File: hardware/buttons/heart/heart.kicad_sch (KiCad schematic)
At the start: 10 parts

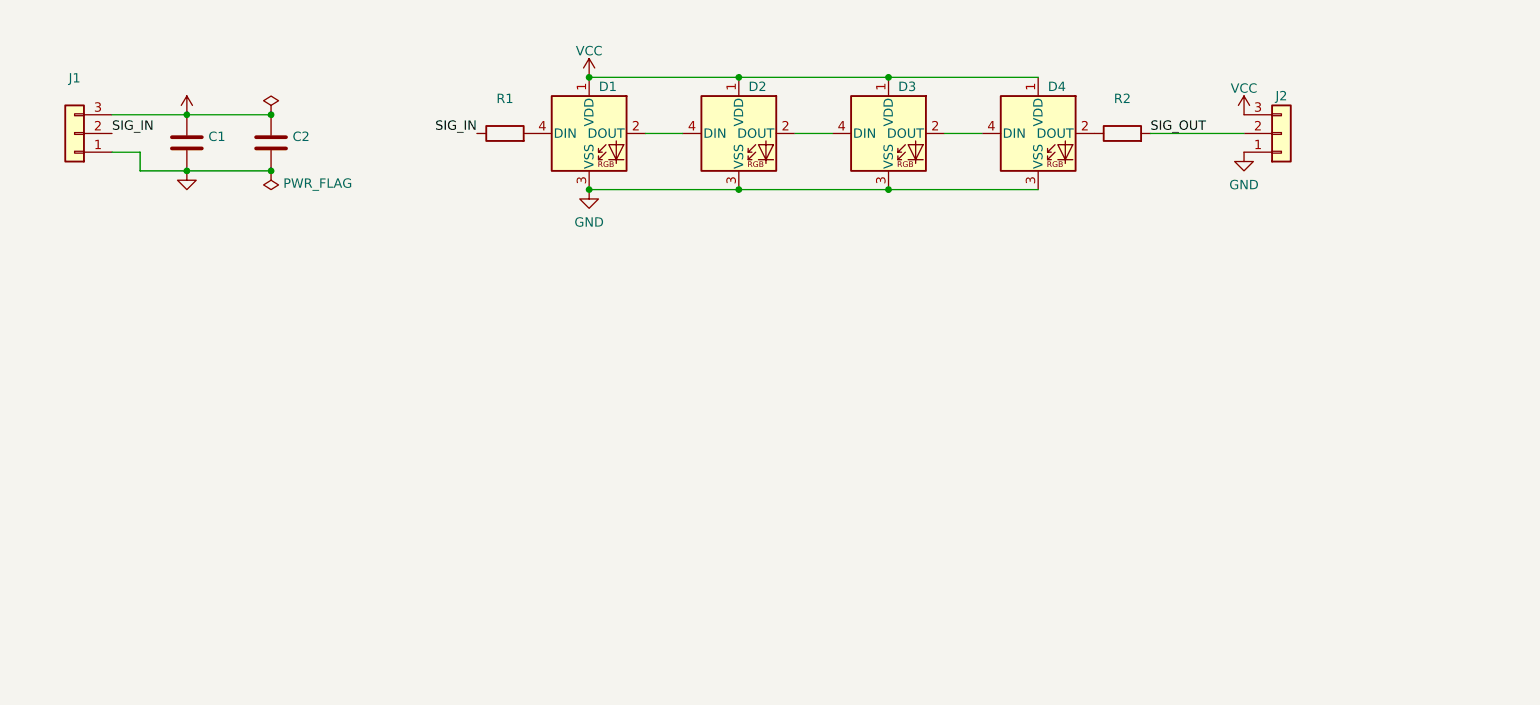
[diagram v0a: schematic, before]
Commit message: Add heart button
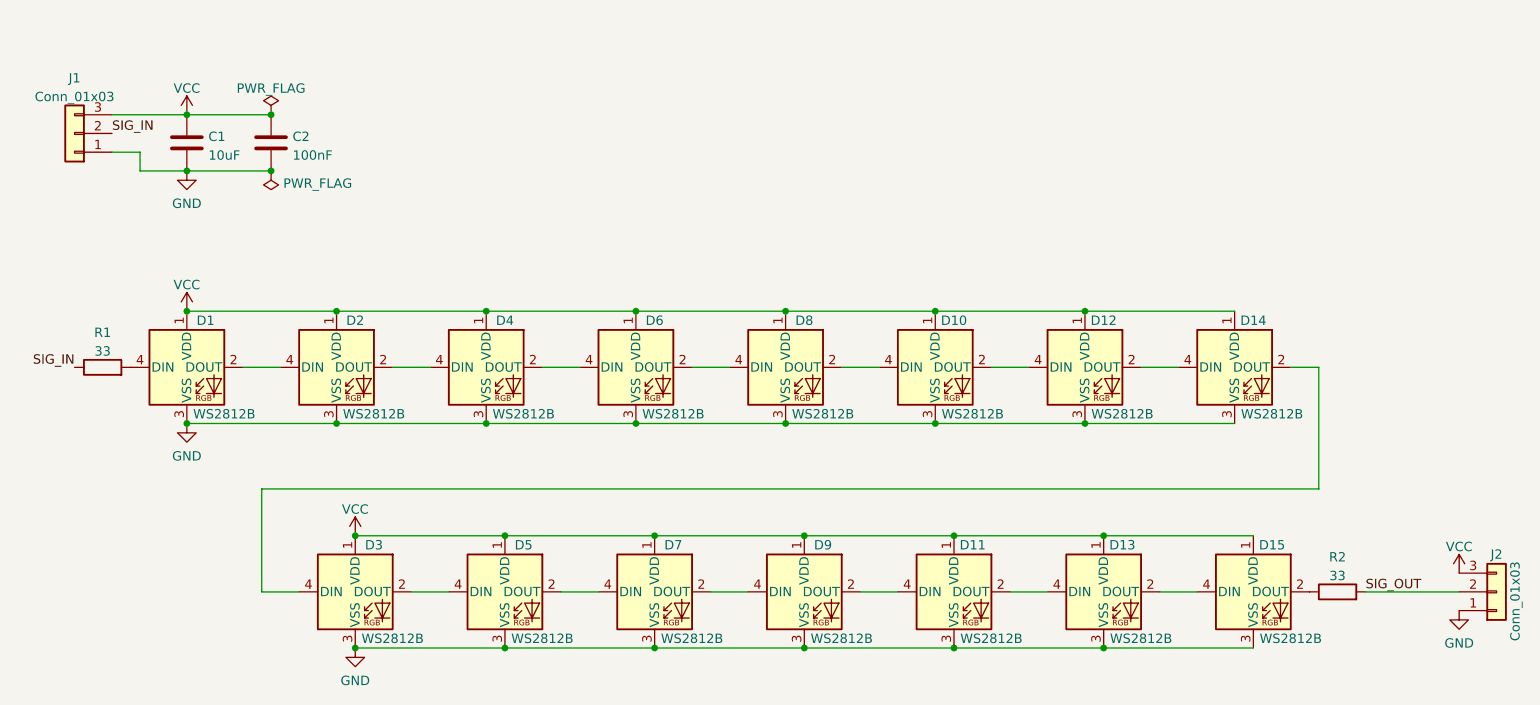
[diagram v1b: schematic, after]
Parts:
- added D10, D11, D12, D13, D14, D15, D3, D5, D7, D8, D9: WS2812B, LED_SMD:LED_WS2812B_PLCC4_5.0x5.0mm_P3.2mm, symbol LED:WS2812B
- C1: value (none) -> 10uF; footprint (none) -> Capacitor_SMD:C_0603_1608Metric
- C2: value (none) -> 100nF; footprint (none) -> Capacitor_SMD:C_0402_1005Metric
- D1, D2: value (none) -> WS2812B; footprint (none) -> LED_SMD:LED_WS2812B_PLCC4_5.0x5.0mm_P3.2mm
- D4: renamed from D3; value (none) -> WS2812B; footprint (none) -> LED_SMD:LED_WS2812B_PLCC4_5.0x5.0mm_P3.2mm
- D6: renamed from D4; value (none) -> WS2812B; footprint (none) -> LED_SMD:LED_WS2812B_PLCC4_5.0x5.0mm_P3.2mm
- J1, J2: value (none) -> Conn_01x03; footprint (none) -> Connector_PinHeader_2.54mm:PinHeader_1x03_P2.54mm_Vertical
- R1, R2: value (none) -> 33; footprint (none) -> Resistor_SMD:R_0603_1608Metric
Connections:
- net GND: now also D10.3 (VSS), D11.3 (VSS), D12.3 (VSS), D13.3 (VSS), D14.3 (VSS), D15.3 (VSS), D3.3 (VSS), D5.3 (VSS), D7.3 (VSS), D8.3 (VSS), D9.3 (VSS)
- net VCC: now also D10.1 (VDD), D11.1 (VDD), D12.1 (VDD), D13.1 (VDD), D14.1 (VDD), D15.1 (VDD), D3.1 (VDD), D5.1 (VDD), D7.1 (VDD), D8.1 (VDD), D9.1 (VDD)
- net at D6.2 (DOUT): now also D8.4 (DIN); no longer R2.1
- new net: D5.2 (DOUT), D7.4 (DIN)
- new net: D3.2 (DOUT), D5.4 (DIN)
- new net: D10.4 (DIN), D8.2 (DOUT)
- new net: D14.2 (DOUT), D3.4 (DIN)
- new net: D11.2 (DOUT), D13.4 (DIN)
- new net: D11.4 (DIN), D9.2 (DOUT)
- new net: D12.2 (DOUT), D14.4 (DIN)
- new net: D13.2 (DOUT), D15.4 (DIN)
- new net: D10.2 (DOUT), D12.4 (DIN)
- new net: D15.2 (DOUT), R2.1
- new net: D7.2 (DOUT), D9.4 (DIN)
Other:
- moved on the sheet: D1, D2, D4, D6, J2, R1, R2

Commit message: Add mounting holes
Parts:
- added H1, H2, H3, H4: (no value), symbol Mechanical:MountingHole
- C1: value 10uF -> (none); footprint Capacitor_SMD:C_0603_1608Metric -> (none)
- C2: value 100nF -> (none); footprint Capacitor_SMD:C_0402_1005Metric -> (none)
- D1, D10, D11, D12, D13, D14, D15, D2, D3, D4, D5, D6, D7, D8, D9: value WS2812B -> (none); footprint LED_SMD:LED_WS2812B_PLCC4_5.0x5.0mm_P3.2mm -> (none)
- J1, J2: value Conn_01x03 -> (none); footprint Connector_PinHeader_2.54mm:PinHeader_1x03_P2.54mm_Vertical -> (none)
- R1, R2: value 33 -> (none); footprint Resistor_SMD:R_0603_1608Metric -> (none)
